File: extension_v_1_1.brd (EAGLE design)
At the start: 68.6 x 53.3 mm, 6 parts

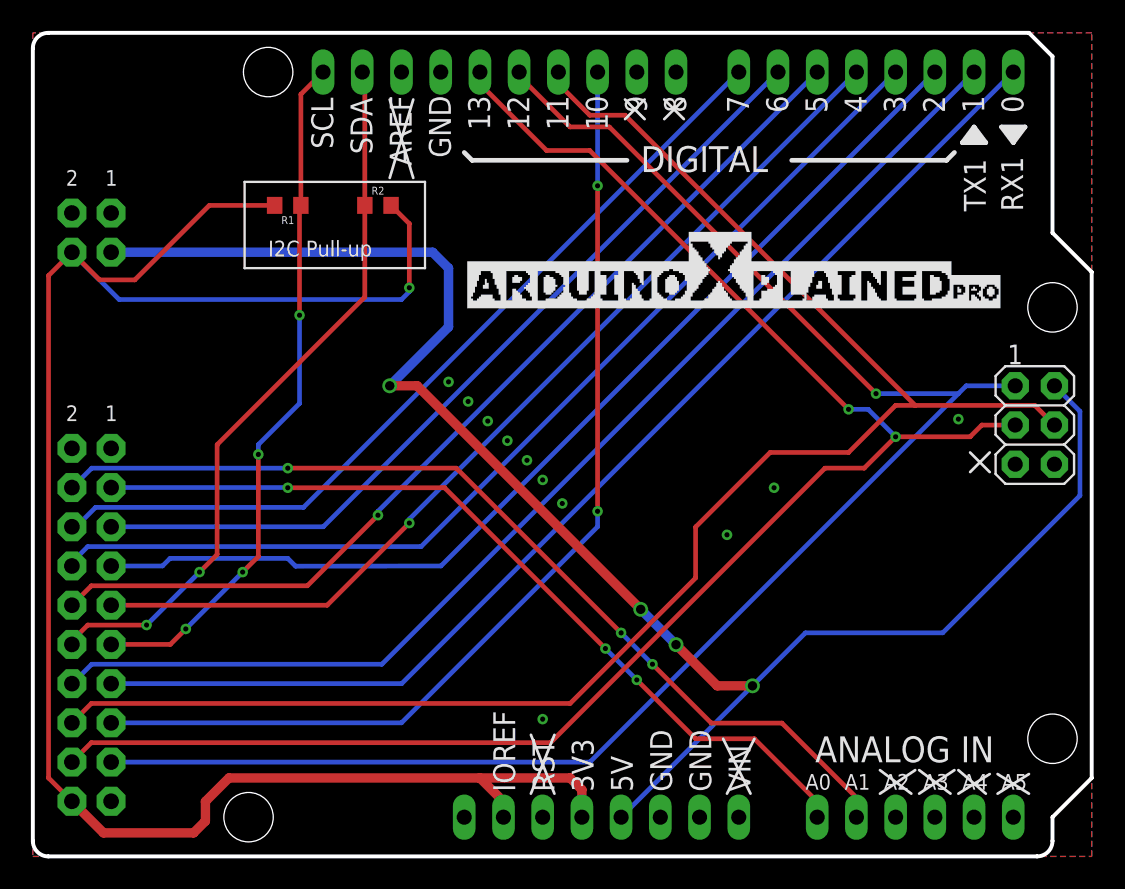
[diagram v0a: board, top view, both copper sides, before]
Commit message: Fixed bug where SDL and SDA pins were interchanged
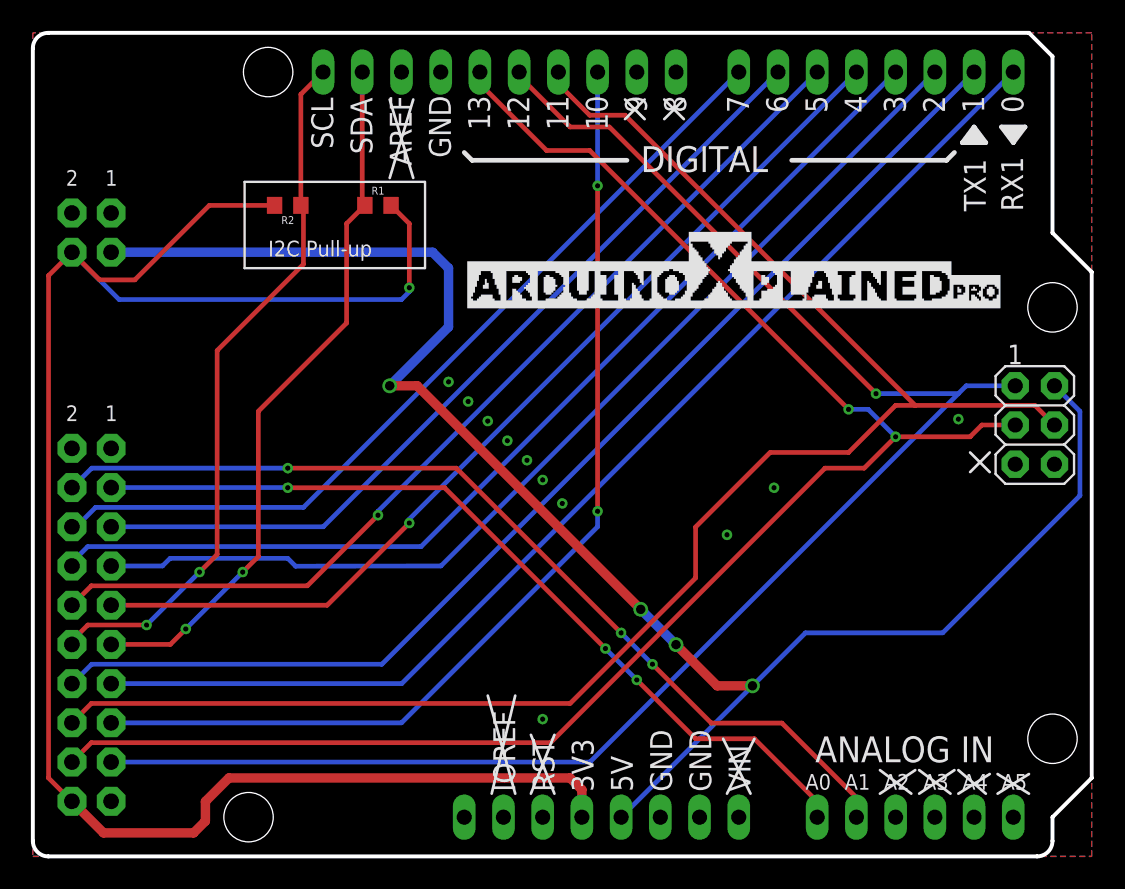
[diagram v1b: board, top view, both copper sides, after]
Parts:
- added U$3: (no value), ihpcb-misc:ELECTRIC_PCB_LOGO
- R1, R2: value N.M. -> NOT MOUNTED
- moved R1 5.84 mm to (22.4, 42.2), turned to 0 degrees
- moved R2 5.84 mm to (16.5, 42.2), turned to 180 degrees
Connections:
- net I2C_SCL: now also U$2.60; no longer U$2.50
- net I2C_SDA: now also U$2.50; no longer U$2.60
- net VCC_3V3: no longer U$2.2
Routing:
- net VCC_3V3: track 123.4 -> 120.3 mm
- net I2C_SDA: track 45.0 -> 46.2 mm, vias 4 -> 2
- net I2C_SCL: track 47.2 -> 46.2 mm
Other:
- board text added: "Revision 1.1 11.03.2015"
- board text removed: "Ivar Holand Revision 1.0 03.12.2013"
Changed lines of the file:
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@@
 <?xml version="1.0" encoding="utf-8"?>
 <!DOCTYPE eagle SYSTEM "eagle.dtd">
-<eagle version="6.4">
+<eagle version="7.2.0">
 <drawing>
 <settings>
@@
 <layer number="27" name="tValues" color="7" fill="1" visible="yes" active="yes"/>
 <layer number="28" name="bValues" color="7" fill="1" visible="yes" active="yes"/>
-<layer number="29" name="tStop" color="7" fill="3" visible="yes" active="yes"/>
-<layer number="30" name="bStop" color="7" fill="6" visible="yes" active="yes"/>
-<layer number="31" name="tCream" color="7" fill="4" visible="yes" active="yes"/>
-<layer number="32" name="bCream" color="7" fill="5" visible="yes" active="yes"/>
-<layer number="33" name="tFinish" color="6" fill="3" visible="yes" active="yes"/>
-<layer number="34" name="bFinish" color="6" fill="6" visible="yes" active="yes"/>
-<layer number="35" name="tGlue" color="7" fill="4" visible="yes" active="yes"/>
-<layer number="36" name="bGlue" color="7" fill="5" visible="yes" active="yes"/>
+<layer number="29" name="tStop" color="7" fill="3" visible="no" active="yes"/>
+<layer number="30" name="bStop" color="7" fill="6" visible="no" active="yes"/>
+<layer number="31" name="tCream" color="7" fill="4" visible="no" active="yes"/>
+<layer number="32" name="bCream" color="7" fill="5" visible="no" active="yes"/>
+<layer number="33" name="tFinish" color="6" fill="3" visible="no" active="yes"/>
+<layer number="34" name="bFinish" color="6" fill="6" visible="no" active="yes"/>
+<layer number="35" name="tGlue" color="7" fill="4" visible="no" active="yes"/>
+<layer number="36" name="bGlue" color="7" fill="5" visible="no" active="yes"/>
 <layer number="37" name="tTest" color="7" fill="1" visible="yes" active="yes"/>
 <layer number="38" name="bTest" color="7" fill="1" visible="yes" active="yes"/>
@@
 <layer number="106" name="bPlate" color="7" fill="1" visible="no" active="no"/>
 <layer number="107" name="Crop" color="7" fill="1" visible="no" active="no"/>
+<layer number="108" name="CONTAINER" color="14" fill="4" visible="yes" active="yes"/>
 <layer number="116" name="Patch_BOT" color="7" fill="1" visible="no" active="no"/>
 <layer number="121" name="_tsilk" color="7" fill="1" visible="no" active="no"/>
@@
 <wire x1="61.976" y1="26.162" x2="60.706" y2="24.892" width="0.1778" layer="21"/>
 <wire x1="61.976" y1="24.892" x2="60.706" y2="26.162" width="0.1778" layer="21"/>
-<text x="65.786" y="15.494" size="1.524" layer="22" ratio="15" rot="MR0">Ivar Holand
-Revision 1.0
-03.12.2013</text>
+<text x="65.786" y="15.494" size="1.524" layer="22" ratio="15" rot="MR0">Revision 1.1
+11.03.2015</text>
 <text x="5.08" y="28.194" size="1.016" layer="21" ratio="15" align="bottom-center">1</text>
 <text x="2.54" y="28.194" size="1.016" layer="21" ratio="15" align="bottom-center">2</text>
 <text x="2.54" y="43.434" size="1.016" layer="21" ratio="15" align="bottom-center">2</text>
 <text x="5.08" y="43.434" size="1.016" layer="21" ratio="15" align="bottom-center">1</text>
+<wire x1="29.718" y1="4.064" x2="31.242" y2="10.414" width="0.1778" layer="21"/>
+<wire x1="31.242" y1="4.064" x2="29.464" y2="10.414" width="0.1778" layer="21"/>
 </plain>
 <attributes>
@@
 <pass name="Default">
 <param name="RoutingGrid" value="50mil"/>
+<param name="AutoGrid" value="1"/>
+<param name="Efforts" value="0"/>
+<param name="TopRouterVariant" value="1"/>
 <param name="tpViaShape" value="round"/>
 <param name="PrefDir.1" value="|"/>
@@
 <element name="U$2" library="ihpcb-arduino" package="STANDARD_NO_PWR" value="ARDUINO_UNO_SIZE_MCU_BOARD_NO_PWR" x="0" y="0"/>
 <element name="PWR" library="ihpcb-pin_header" package="H4X2_100_MIL" value="M02X2" x="3.8" y="40.4" rot="MR0"/>
-<element name="R1" library="ihpcb-res_cap" package="0603" value="N.M." x="16.51" y="42.164" rot="R180"/>
-<element name="R2" library="ihpcb-res_cap" package="0603" value="N.M." x="22.352" y="42.164"/>
+<element name="R1" library="ihpcb-res_cap" package="0603" value="NOT MOUNTED" x="22.352" y="42.164"/>
+<element name="R2" library="ihpcb-res_cap" package="0603" value="NOT MOUNTED" x="16.51" y="42.164" rot="R180"/>
 <element name="U$1" library="ihpcb-misc" package="ARDUINOXPLAINEDPRO" value="" x="28.194" y="35.56"/>
+<element name="U$3" library="ihpcb-misc" package="ELECTRIC_PCB_LOGO" value="" x="24.384" y="7.112" rot="MR0"/>
 </elements>
 <signals>
@@
 <signal name="I2C_SDA">
 <contactref element="EXT1" pad="11"/>
-<contactref element="U$2" pad="60"/>
+<contactref element="U$2" pad="50"/>
 <contactref element="R1" pad="1"/>
-<wire x1="18.796" y1="50.8" x2="17.36" y2="49.364" width="0.3048" layer="1"/>
-<wire x1="17.36" y1="49.364" x2="17.36" y2="42.164" width="0.3048" layer="1"/>
 <wire x1="5.07" y1="13.73" x2="8.904" y2="13.73" width="0.3048" layer="1"/>
 <wire x1="8.904" y1="13.73" x2="9.906" y2="14.732" width="0.3048" layer="1"/>
@@
 <via x="13.589" y="18.415" extent="1-16" drill="0.3302"/>
 <wire x1="13.589" y1="18.415" x2="14.605" y2="19.431" width="0.3048" layer="1"/>
-<wire x1="14.605" y1="19.431" x2="14.605" y2="26.035" width="0.3048" layer="1"/>
-<via x="14.605" y="26.035" extent="1-16" drill="0.3302"/>
-<wire x1="14.605" y1="26.035" x2="14.605" y2="26.67" width="0.3048" layer="16"/>
-<wire x1="14.605" y1="26.67" x2="17.272" y2="29.337" width="0.3048" layer="16"/>
-<wire x1="17.272" y1="29.337" x2="17.272" y2="35.052" width="0.3048" layer="16"/>
-<via x="17.272" y="35.052" extent="1-16" drill="0.3302"/>
-<wire x1="17.36" y1="42.164" x2="17.272" y2="42.076" width="0.3048" layer="1"/>
-<wire x1="17.272" y1="42.076" x2="17.272" y2="35.052" width="0.3048" layer="1"/>
+<wire x1="14.605" y1="19.431" x2="14.605" y2="28.829" width="0.3048" layer="1"/>
+<wire x1="14.605" y1="28.829" x2="20.32" y2="34.544" width="0.3048" layer="1"/>
+<wire x1="20.32" y1="34.544" x2="20.32" y2="40.982" width="0.3048" layer="1"/>
+<wire x1="20.32" y1="40.982" x2="21.502" y2="42.164" width="0.3048" layer="1"/>
+<wire x1="21.336" y1="50.8" x2="21.336" y2="42.33" width="0.3048" layer="1"/>
+<wire x1="21.336" y1="42.33" x2="21.502" y2="42.164" width="0.3048" layer="1"/>
 </signal>
 <signal name="USART_RX">
@@
 <signal name="I2C_SCL">
 <contactref element="EXT1" pad="12"/>
-<contactref element="U$2" pad="50"/>
+<contactref element="U$2" pad="60"/>
 <contactref element="R2" pad="1"/>
-<wire x1="21.336" y1="50.8" x2="21.502" y2="50.634" width="0.3048" layer="1"/>
-<wire x1="21.502" y1="50.634" x2="21.502" y2="42.164" width="0.3048" layer="1"/>
 <wire x1="2.53" y1="13.73" x2="2.53" y2="13.96" width="0.3048" layer="1"/>
 <wire x1="2.53" y1="13.96" x2="3.556" y2="14.986" width="0.3048" layer="1"/>
@@
 <via x="10.795" y="18.415" extent="1-16" drill="0.3302"/>
 <wire x1="10.795" y1="18.415" x2="11.938" y2="19.558" width="0.3048" layer="1"/>
-<wire x1="11.938" y1="19.558" x2="11.938" y2="26.67" width="0.3048" layer="1"/>
-<wire x1="11.938" y1="26.67" x2="21.502" y2="36.234" width="0.3048" layer="1"/>
-<wire x1="21.502" y1="36.234" x2="21.502" y2="42.164" width="0.3048" layer="1"/>
+<wire x1="11.938" y1="19.558" x2="11.938" y2="32.766" width="0.3048" layer="1"/>
+<wire x1="11.938" y1="32.766" x2="17.526" y2="38.354" width="0.3048" layer="1"/>
+<wire x1="17.526" y1="38.354" x2="17.526" y2="41.998" width="0.3048" layer="1"/>
+<wire x1="17.526" y1="41.998" x2="17.36" y2="42.164" width="0.3048" layer="1"/>
+<wire x1="17.36" y1="42.164" x2="17.36" y2="49.364" width="0.3048" layer="1"/>
+<wire x1="17.36" y1="49.364" x2="18.796" y2="50.8" width="0.3048" layer="1"/>
 </signal>
 <signal name="USART_TX">
@@
 <contactref element="EXT1" pad="20"/>
 <contactref element="U$2" pad="4"/>
-<contactref element="U$2" pad="2"/>
 <contactref element="PWR" pad="4"/>
 <contactref element="R1" pad="2"/>
@@
 <wire x1="11.176" y1="2.286" x2="11.176" y2="3.556" width="0.6096" layer="1"/>
 <wire x1="11.176" y1="3.556" x2="12.7" y2="5.08" width="0.6096" layer="1"/>
-<wire x1="12.7" y1="5.08" x2="28.956" y2="5.08" width="0.6096" layer="1"/>
-<wire x1="28.956" y1="5.08" x2="30.48" y2="3.556" width="0.6096" layer="1"/>
-<wire x1="30.48" y1="3.556" x2="30.48" y2="2.54" width="0.6096" layer="1"/>
+<wire x1="12.7" y1="5.08" x2="34.798" y2="5.08" width="0.6096" layer="1"/>
 <wire x1="2.53" y1="39.13" x2="1.016" y2="37.616" width="0.3048" layer="1"/>
 <wire x1="1.016" y1="37.616" x2="1.016" y2="5.08" width="0.3048" layer="1"/>
@@
 <wire x1="4.322" y1="37.338" x2="6.604" y2="37.338" width="0.3048" layer="1"/>
 <wire x1="6.604" y1="37.338" x2="11.43" y2="42.164" width="0.3048" layer="1"/>
-<wire x1="11.43" y1="42.164" x2="15.66" y2="42.164" width="0.3048" layer="1"/>
-<wire x1="23.202" y1="42.164" x2="24.384" y2="40.982" width="0.3048" layer="1"/>
 <wire x1="24.384" y1="40.982" x2="24.384" y2="36.83" width="0.3048" layer="1"/>
 <via x="24.384" y="36.83" extent="1-16" drill="0.3302"/>
@@
 <wire x1="35.56" y1="2.54" x2="35.56" y2="4.318" width="0.6096" layer="1"/>
 <wire x1="35.56" y1="4.318" x2="34.798" y2="5.08" width="0.6096" layer="1"/>
-<wire x1="34.798" y1="5.08" x2="28.956" y2="5.08" width="0.6096" layer="1"/>
+<wire x1="11.43" y1="42.164" x2="15.66" y2="42.164" width="0.3048" layer="1"/>
+<wire x1="24.384" y1="40.982" x2="23.202" y2="42.164" width="0.3048" layer="1"/>
 <wire x1="2.53" y1="39.13" x2="2.54" y2="39.116" width="0" layer="19" extent="16-16"/>
 </signal>
